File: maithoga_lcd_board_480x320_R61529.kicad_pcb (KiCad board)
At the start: 2 copper layers, 15 parts, among them P1 Display Connector, P2 40pin_fpc_top_0_5mm, U1 TSC2007, U2 DIO5661ST6

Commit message: Schematic ready, need check
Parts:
- added P3: TouchXY Connector, Goldpin:Goldpin_4_2_2_54mm_SMT, F.Cu at (138.4, 110.5)
- P2: value 40pin_fpc_top_0_5mm -> LicheePi_Con
- moved U1 24.8 mm to (177.8, 88.3)
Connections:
- C3 pad 1: /Display and Touchscreen/LCD Backlight/LCD_LED_A -> /Display and Touchscreen/LCD_LED_A
- D2 pad 1: /Display and Touchscreen/LCD Backlight/LCD_LED_A -> /Display and Touchscreen/LCD_LED_A
- DIS1 pad 1: /Display and Touchscreen/LCD Backlight/LCD_LED_K -> /Display and Touchscreen/LCD_LED_K
- DIS1 pad 11: (no net) -> /Display and Touchscreen/DISP_TE
- DIS1 pad 12: (no net) -> /Display and Touchscreen/DISP_~CS~
- DIS1 pad 13: (no net) -> /Display and Touchscreen/DISP_RS
- DIS1 pad 14: (no net) -> /Display and Touchscreen/DISP_~WR~
- DIS1 pad 15: (no net) -> /Display and Touchscreen/DISP_~RD~
- DIS1 pad 16: (no net) -> /Display and Touchscreen/DISP_SDA
- DIS1 pad 17: (no net) -> /Display and Touchscreen/DISP_SDO
- DIS1 pad 18: (no net) -> /Display and Touchscreen/DISP_D0
- DIS1 pad 19: (no net) -> /Display and Touchscreen/DISP_D1
- DIS1 pad 2: /Display and Touchscreen/LCD Backlight/LCD_LED_K -> /Display and Touchscreen/LCD_LED_K
- DIS1 pad 20: (no net) -> /Display and Touchscreen/DISP_D2
- DIS1 pad 21: (no net) -> /Display and Touchscreen/DISP_D3
- DIS1 pad 22: (no net) -> /Display and Touchscreen/DISP_D4
- DIS1 pad 23: (no net) -> /Display and Touchscreen/DISP_D5
- DIS1 pad 24: (no net) -> /Display and Touchscreen/DISP_D6
- DIS1 pad 25: (no net) -> /Display and Touchscreen/DISP_D7
- DIS1 pad 26: (no net) -> /Display and Touchscreen/DISP_D8
- DIS1 pad 27: (no net) -> /Display and Touchscreen/DISP_D9
- DIS1 pad 28: (no net) -> /Display and Touchscreen/DISP_D10
- DIS1 pad 29: (no net) -> /Display and Touchscreen/DISP_D11
- DIS1 pad 3: /Display and Touchscreen/LCD Backlight/LCD_LED_K -> /Display and Touchscreen/LCD_LED_K
- DIS1 pad 30: (no net) -> /Display and Touchscreen/DISP_D12
- DIS1 pad 31: (no net) -> /Display and Touchscreen/DISP_D13
- DIS1 pad 32: (no net) -> /Display and Touchscreen/DISP_D14
- DIS1 pad 33: (no net) -> /Display and Touchscreen/DISP_D15
- DIS1 pad 34: (no net) -> /Display and Touchscreen/DISP_D16
- DIS1 pad 35: (no net) -> /Display and Touchscreen/DISP_D17
- DIS1 pad 36: (no net) -> /Display and Touchscreen/DISP_ENABLE
- DIS1 pad 37: (no net) -> /Display and Touchscreen/DISP_DOTCLK
- DIS1 pad 38: (no net) -> /Display and Touchscreen/DISP_HSYNC
- DIS1 pad 4: /Display and Touchscreen/LCD Backlight/LCD_LED_K -> /Display and Touchscreen/LCD_LED_K
- DIS1 pad 40: (no net) -> /Display and Touchscreen/DISP_VSYNC
- DIS1 pad 41: (no net) -> /Display and Touchscreen/DISP_~RESET~
- DIS1 pad 46: Net-(DIS1-Pad46) -> /Lichee Pi Display Connector/TPX1
- DIS1 pad 47: Net-(DIS1-Pad47) -> /Lichee Pi Display Connector/TPX2
- DIS1 pad 48: Net-(DIS1-Pad48) -> /Lichee Pi Display Connector/TPY1
- DIS1 pad 49: Net-(DIS1-Pad49) -> /Lichee Pi Display Connector/TPY2
- DIS1 pad 5: /Display and Touchscreen/LCD Backlight/LCD_LED_K -> /Display and Touchscreen/LCD_LED_K
- DIS1 pad 6: /Display and Touchscreen/LCD Backlight/LCD_LED_K -> /Display and Touchscreen/LCD_LED_K
- DIS1 pad 7: /Display and Touchscreen/LCD Backlight/LCD_LED_A -> /Display and Touchscreen/LCD_LED_A
- P1 pad 1: (no net) -> 3V3
- P1 pad 10: (no net) -> /Display and Touchscreen/DISP_SDA
- P1 pad 11: (no net) -> /Display and Touchscreen/DISP_SDO
- P1 pad 12: (no net) -> /Display and Touchscreen/DISP_D0
- P1 pad 13: (no net) -> /Display and Touchscreen/DISP_D1
- P1 pad 14: (no net) -> /Display and Touchscreen/DISP_D2
- P1 pad 15: (no net) -> /Display and Touchscreen/DISP_D3
- P1 pad 16: (no net) -> /Display and Touchscreen/DISP_D4
- P1 pad 17: (no net) -> /Display and Touchscreen/DISP_D5
- P1 pad 18: (no net) -> /Display and Touchscreen/DISP_D6
- P1 pad 19: (no net) -> /Display and Touchscreen/DISP_D7
- P1 pad 2: (no net) -> GND
- P1 pad 20: (no net) -> /Display and Touchscreen/DISP_D8
- P1 pad 21: (no net) -> /Display and Touchscreen/DISP_D9
- P1 pad 22: (no net) -> /Display and Touchscreen/DISP_D10
- P1 pad 23: (no net) -> /Display and Touchscreen/DISP_D11
- P1 pad 24: (no net) -> /Display and Touchscreen/DISP_D12
- P1 pad 25: (no net) -> /Display and Touchscreen/DISP_D13
- P1 pad 26: (no net) -> /Display and Touchscreen/DISP_D14
- P1 pad 27: (no net) -> /Display and Touchscreen/DISP_D15
- P1 pad 28: (no net) -> /Display and Touchscreen/DISP_D16
- P1 pad 29: (no net) -> /Display and Touchscreen/DISP_D17
- P1 pad 3: (no net) -> /Display and Touchscreen/LCD_LED_K
- P1 pad 30: (no net) -> /Display and Touchscreen/DISP_ENABLE
- P1 pad 31: (no net) -> /Display and Touchscreen/DISP_DOTCLK
- P1 pad 32: (no net) -> /Display and Touchscreen/DISP_HSYNC
- P1 pad 33: (no net) -> /Display and Touchscreen/DISP_VSYNC
- P1 pad 34: (no net) -> /Display and Touchscreen/DISP_~RESET~
- P1 pad 35: (no net) -> /Display and Touchscreen/TOUCHSCREEN_SDA
- P1 pad 36: (no net) -> /Display and Touchscreen/TOUCHSCREEN_SCL
- P1 pad 37: (no net) -> 3V3
- P1 pad 38: (no net) -> GND
- P1 pad 39: (no net) -> /Display and Touchscreen/TOUCHSCREEN_IRQ
- P1 pad 4: (no net) -> /Display and Touchscreen/LCD_LED_A
- P1 pad 40: (no net) -> /Display and Touchscreen/BACKLIGHT_PWM
- P1 pad 5: (no net) -> /Display and Touchscreen/DISP_TE
- P1 pad 6: (no net) -> /Display and Touchscreen/DISP_~CS~
- P1 pad 7: (no net) -> /Display and Touchscreen/DISP_RS
- P1 pad 8: (no net) -> /Display and Touchscreen/DISP_~WR~
- P1 pad 9: (no net) -> /Display and Touchscreen/DISP_~RD~
- P2 pad 1: (no net) -> /Display and Touchscreen/LCD_LED_K
- P2 pad 10: (no net) -> /Display and Touchscreen/DISP_D3
- P2 pad 11: (no net) -> /Display and Touchscreen/DISP_D4
- P2 pad 12: (no net) -> /Display and Touchscreen/DISP_D5
- P2 pad 13: (no net) -> GND
- P2 pad 14: (no net) -> GND
- P2 pad 15: (no net) -> /Display and Touchscreen/DISP_D6
- P2 pad 16: (no net) -> /Display and Touchscreen/DISP_D7
- P2 pad 17: (no net) -> /Display and Touchscreen/DISP_D8
- P2 pad 18: (no net) -> /Display and Touchscreen/DISP_D9
- P2 pad 19: (no net) -> /Display and Touchscreen/DISP_D10
- P2 pad 2: (no net) -> /Display and Touchscreen/LCD_LED_A
- P2 pad 20: (no net) -> /Display and Touchscreen/DISP_D11
- P2 pad 21: (no net) -> GND
- P2 pad 22: (no net) -> GND
- P2 pad 23: (no net) -> /Display and Touchscreen/DISP_D12
- P2 pad 24: (no net) -> /Display and Touchscreen/DISP_D13
- P2 pad 25: (no net) -> /Display and Touchscreen/DISP_D14
- P2 pad 26: (no net) -> /Display and Touchscreen/DISP_D15
- P2 pad 27: (no net) -> /Display and Touchscreen/DISP_D16
- P2 pad 28: (no net) -> /Display and Touchscreen/DISP_D17
- P2 pad 29: (no net) -> GND
- P2 pad 3: (no net) -> GND
- P2 pad 30: (no net) -> /Display and Touchscreen/DISP_DOTCLK
- P2 pad 31: (no net) -> 3V3
- P2 pad 32: (no net) -> /Display and Touchscreen/DISP_HSYNC
- P2 pad 33: (no net) -> /Display and Touchscreen/DISP_VSYNC
- P2 pad 34: (no net) -> /Display and Touchscreen/DISP_ENABLE
- P2 pad 36: (no net) -> GND
- P2 pad 37: (no net) -> /Lichee Pi Display Connector/TPX1
- P2 pad 38: (no net) -> /Lichee Pi Display Connector/TPY1
- P2 pad 39: (no net) -> /Lichee Pi Display Connector/TPX2
- P2 pad 4: (no net) -> 3V3
- P2 pad 40: (no net) -> /Lichee Pi Display Connector/TPY2
- P2 pad 5: (no net) -> GND
- P2 pad 6: (no net) -> GND
- P2 pad 7: (no net) -> /Display and Touchscreen/DISP_D0
- P2 pad 8: (no net) -> /Display and Touchscreen/DISP_D1
- P2 pad 9: (no net) -> /Display and Touchscreen/DISP_D2
- R4 pad 1: /Display and Touchscreen/LCD Backlight/LCD_LED_K -> /Display and Touchscreen/LCD_LED_K
- U1 pad 2: Net-(DIS1-Pad46) -> /Lichee Pi Display Connector/TPX1
- U1 pad 3: Net-(DIS1-Pad48) -> /Lichee Pi Display Connector/TPY1
- U1 pad 4: Net-(DIS1-Pad47) -> /Lichee Pi Display Connector/TPX2
- U1 pad 5: Net-(DIS1-Pad49) -> /Lichee Pi Display Connector/TPY2
- U2 pad 3: /Display and Touchscreen/LCD Backlight/LCD_LED_K -> /Display and Touchscreen/LCD_LED_K
- U2 pad 4: (no net) -> /Display and Touchscreen/BACKLIGHT_PWM

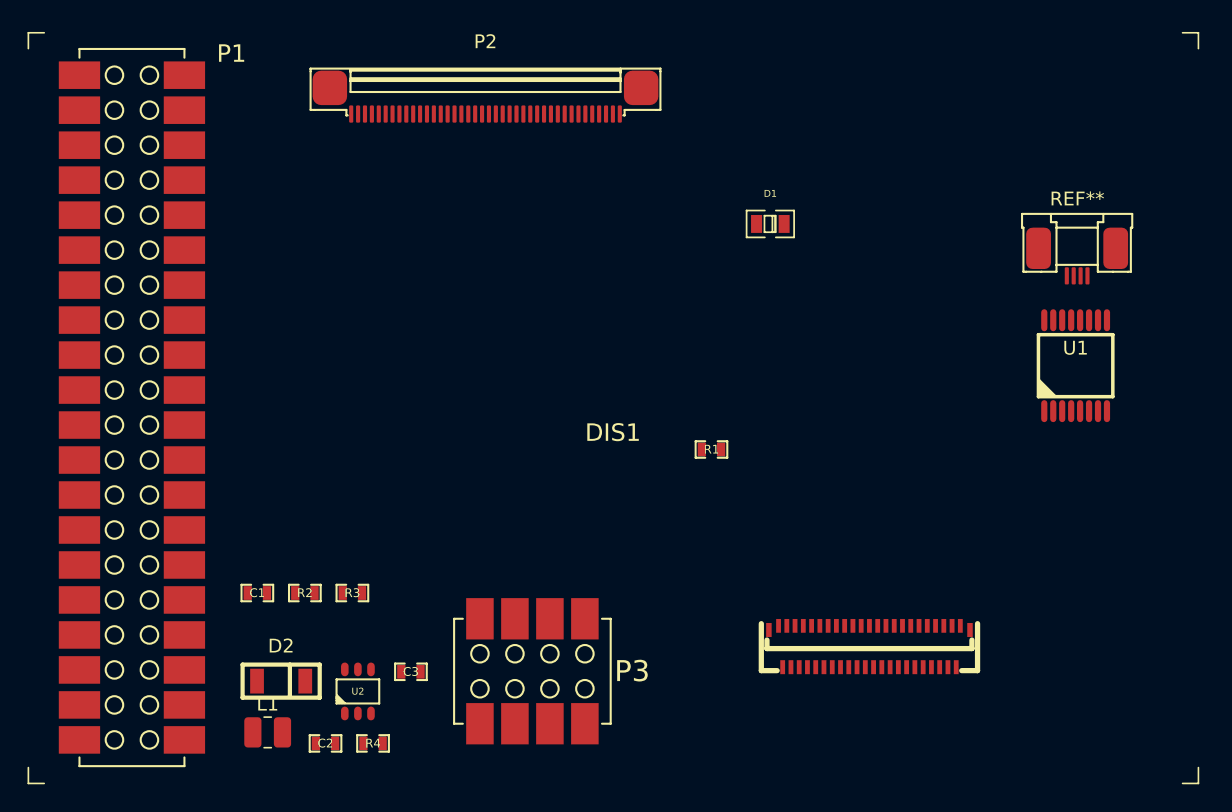
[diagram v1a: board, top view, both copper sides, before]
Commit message: Schematic finished, pcb tracking started
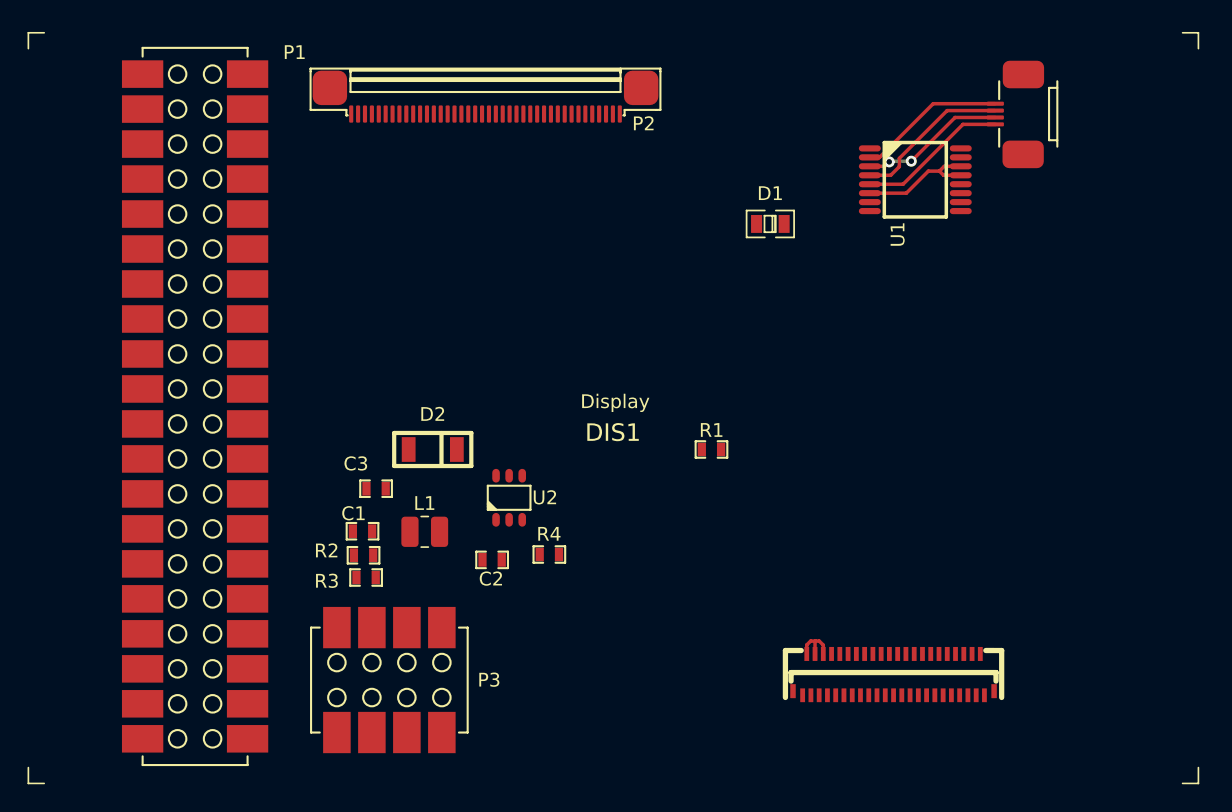
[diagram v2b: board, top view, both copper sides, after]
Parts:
- moved D2 20.1 mm to (131.2, 94.4)
- moved R4 18.8 mm to (139.6, 102.0)
- moved L1 18.5 mm to (130.6, 100.4)
- moved C2 18.0 mm to (135.5, 102.4)
- moved U2 17.8 mm to (136.7, 97.9)
- moved U1 17.8 mm to (166.2, 74.8), turned to 270 degrees
- moved C3 13.5 mm to (127.0, 97.3)
- moved P3 10.4 mm to (128.0, 111.2)
- moved C1 8.85 mm to (126.0, 100.3)
- moved R2 5.07 mm to (126.1, 102.1)
- moved P1 4.59 mm to (113.9, 91.3)
- moved R3 1.50 mm to (126.3, 103.7)
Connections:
- P2 pad 1: /Display and Touchscreen/LCD_LED_K -> /Lichee Pi Display Connector/TPY2
- P2 pad 10: /Display and Touchscreen/DISP_D3 -> 3V3
- P2 pad 11: /Display and Touchscreen/DISP_D4 -> /Display and Touchscreen/DISP_DOTCLK
- P2 pad 12: /Display and Touchscreen/DISP_D5 -> GND
- P2 pad 13: GND -> /Display and Touchscreen/DISP_D17
- P2 pad 14: GND -> /Display and Touchscreen/DISP_D16
- P2 pad 15: /Display and Touchscreen/DISP_D6 -> /Display and Touchscreen/DISP_D15
- P2 pad 16: /Display and Touchscreen/DISP_D7 -> /Display and Touchscreen/DISP_D14
- P2 pad 17: /Display and Touchscreen/DISP_D8 -> /Display and Touchscreen/DISP_D13
- P2 pad 18: /Display and Touchscreen/DISP_D9 -> /Display and Touchscreen/DISP_D12
- P2 pad 19: /Display and Touchscreen/DISP_D10 -> GND
- P2 pad 2: /Display and Touchscreen/LCD_LED_A -> /Lichee Pi Display Connector/TPX2
- P2 pad 20: /Display and Touchscreen/DISP_D11 -> GND
- P2 pad 21: GND -> /Display and Touchscreen/DISP_D11
- P2 pad 22: GND -> /Display and Touchscreen/DISP_D10
- P2 pad 23: /Display and Touchscreen/DISP_D12 -> /Display and Touchscreen/DISP_D9
- P2 pad 24: /Display and Touchscreen/DISP_D13 -> /Display and Touchscreen/DISP_D8
- P2 pad 25: /Display and Touchscreen/DISP_D14 -> /Display and Touchscreen/DISP_D7
- P2 pad 26: /Display and Touchscreen/DISP_D15 -> /Display and Touchscreen/DISP_D6
- P2 pad 27: /Display and Touchscreen/DISP_D16 -> GND
- P2 pad 28: /Display and Touchscreen/DISP_D17 -> GND
- P2 pad 29: GND -> /Display and Touchscreen/DISP_D5
- P2 pad 3: GND -> /Lichee Pi Display Connector/TPY1
- P2 pad 30: /Display and Touchscreen/DISP_DOTCLK -> /Display and Touchscreen/DISP_D4
- P2 pad 31: 3V3 -> /Display and Touchscreen/DISP_D3
- P2 pad 32: /Display and Touchscreen/DISP_HSYNC -> /Display and Touchscreen/DISP_D2
- P2 pad 33: /Display and Touchscreen/DISP_VSYNC -> /Display and Touchscreen/DISP_D1
- P2 pad 34: /Display and Touchscreen/DISP_ENABLE -> /Display and Touchscreen/DISP_D0
- P2 pad 35: (no net) -> GND
- P2 pad 37: /Lichee Pi Display Connector/TPX1 -> 3V3
- P2 pad 38: /Lichee Pi Display Connector/TPY1 -> GND
- P2 pad 39: /Lichee Pi Display Connector/TPX2 -> /Display and Touchscreen/LCD_LED_A
- P2 pad 4: 3V3 -> /Lichee Pi Display Connector/TPX1
- P2 pad 40: /Lichee Pi Display Connector/TPY2 -> /Display and Touchscreen/LCD_LED_K
- P2 pad 6: GND -> (no net)
- P2 pad 7: /Display and Touchscreen/DISP_D0 -> /Display and Touchscreen/DISP_ENABLE
- P2 pad 8: /Display and Touchscreen/DISP_D1 -> /Display and Touchscreen/DISP_VSYNC
- P2 pad 9: /Display and Touchscreen/DISP_D2 -> /Display and Touchscreen/DISP_HSYNC
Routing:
- net /Lichee Pi Display Connector/TPX2: track 0.00 -> 11.4 mm
- net /Lichee Pi Display Connector/TPY2: track 0.00 -> 10.9 mm
- net /Lichee Pi Display Connector/TPX1: track 0.00 -> 10.7 mm
- net /Lichee Pi Display Connector/TPY1: track 0.00 -> 10.6 mm, vias 0 -> 2
- net GND: track 0.00 -> 9.08 mm
- net /Display and Touchscreen/LCD_LED_K: track 0.00 -> 3.69 mm
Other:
- net class Default: trace_width 0.25 -> 0.254

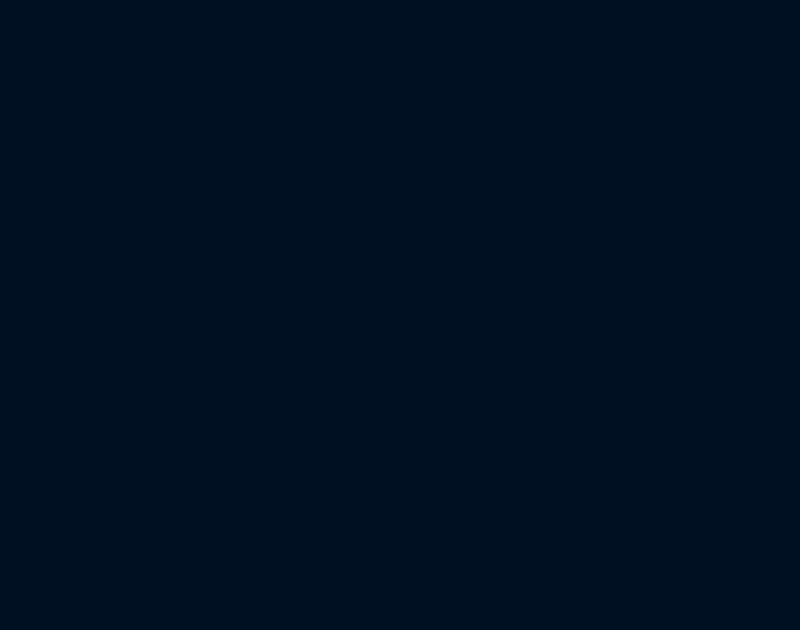
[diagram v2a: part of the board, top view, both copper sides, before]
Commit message: Added resistor mode select on schematic
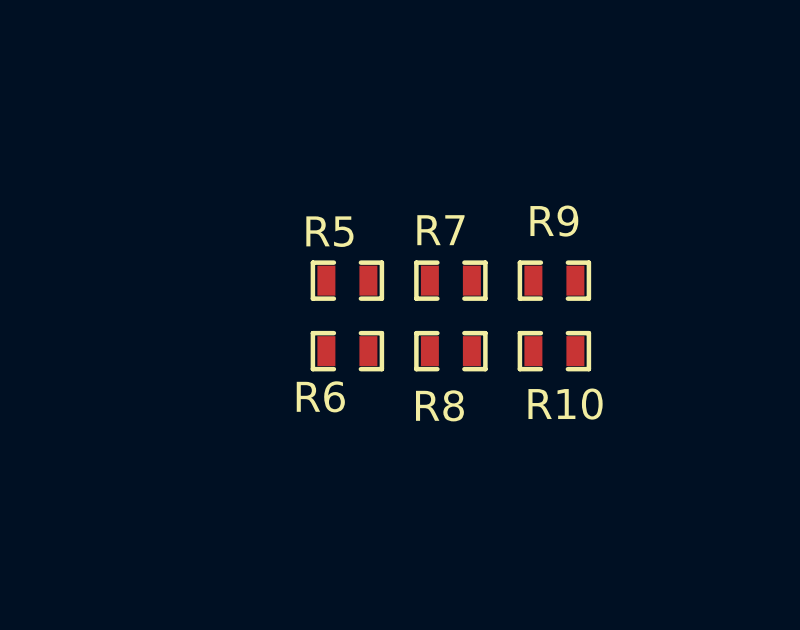
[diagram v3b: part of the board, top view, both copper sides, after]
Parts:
- added R10: 0R, Resistor_Smd_0603:0R_0603, F.Cu at (180.6, 98.0)
- added R5: 0R_NA, Resistor_Smd_0603:0R_0603, F.Cu at (173.7, 95.7)
- added R6: 0R_NA, Resistor_Smd_0603:0R_0603, F.Cu at (173.7, 98.0)
- added R7: 0R, Resistor_Smd_0603:0R_0603, F.Cu at (177.2, 95.7)
- added R8: 0R_NA, Resistor_Smd_0603:0R_0603, F.Cu at (177.2, 98.0)
- added R9: 0R, Resistor_Smd_0603:0R_0603, F.Cu at (180.6, 95.7)
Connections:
- DIS1 pad 42: Net-(D1-Pad2) -> Net-(DIS1-Pad42)
- DIS1 pad 43: Net-(D1-Pad2) -> Net-(DIS1-Pad43)
- DIS1 pad 44: GND -> Net-(DIS1-Pad44)

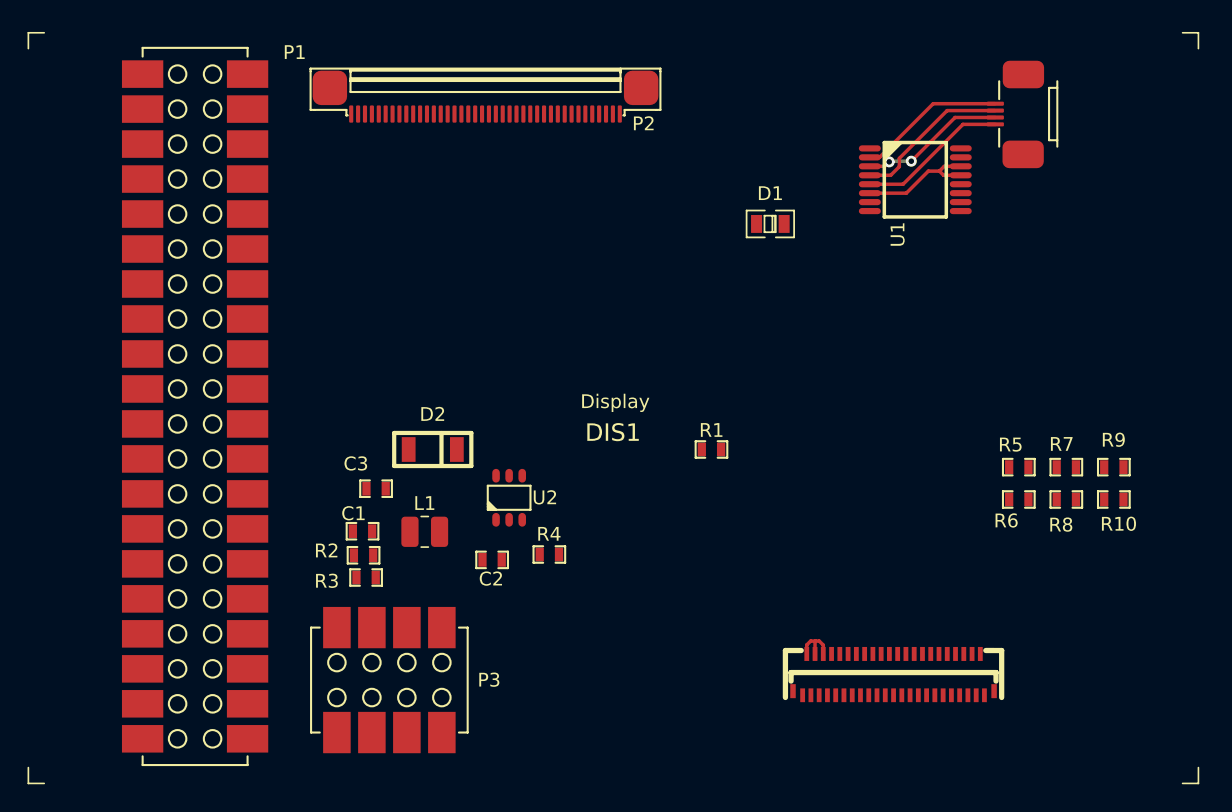
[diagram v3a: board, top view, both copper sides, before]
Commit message: Added outline on pcb
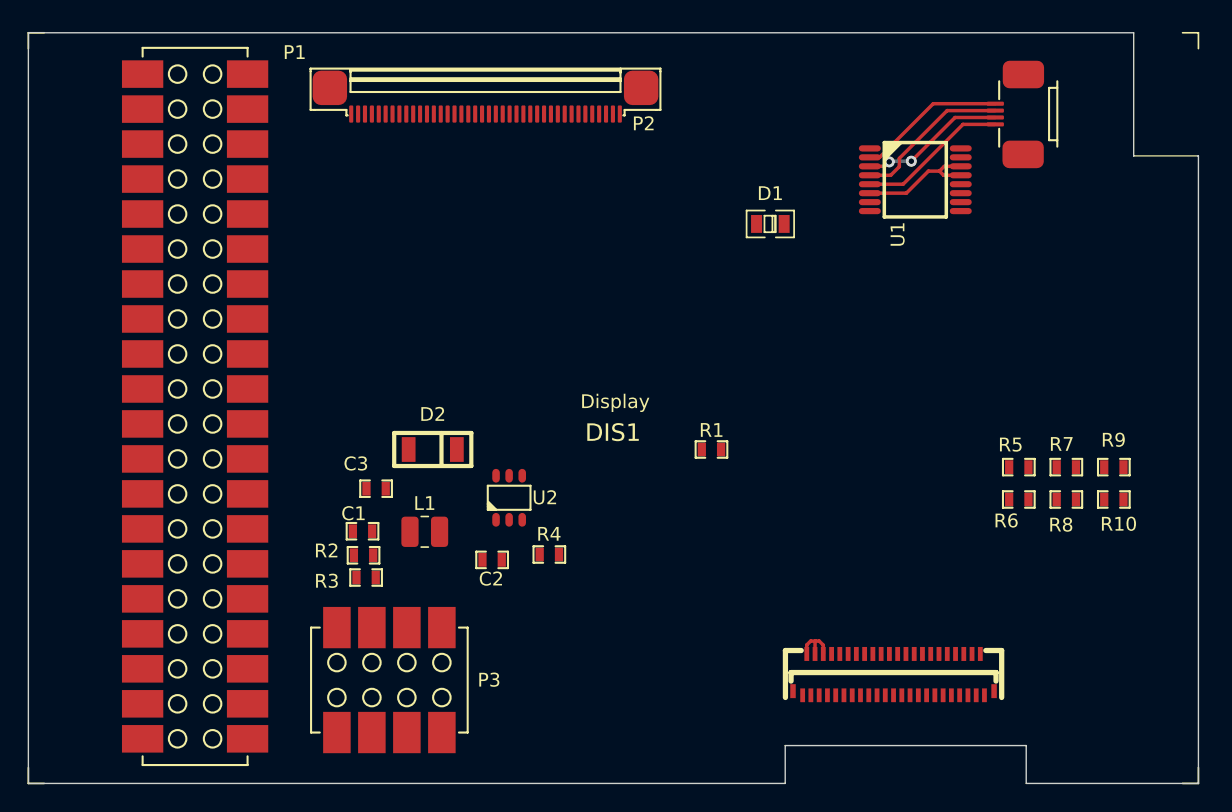
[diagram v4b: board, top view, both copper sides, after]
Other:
- board outline added: 85 x 54.5 mm

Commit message: Tracking in progress
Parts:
- moved R2 51.8 mm to (171.3, 76.7), turned to 90 degrees
- moved R3 49.3 mm to (168.6, 78.4)
- moved C1 46.4 mm to (161.9, 71.0), turned to 90 degrees
- moved C3 31.7 mm to (155.8, 110.4), turned to 90 degrees
- moved D1 28.2 mm to (162.1, 105.5), turned to 270 degrees
- moved R1 27.7 mm to (172.7, 76.7), turned to 90 degrees
- moved D2 27.1 mm to (153.8, 109.4), turned to 270 degrees
- moved L1 23.5 mm to (153.8, 104.3), turned to 270 degrees
- moved U2 22.2 mm to (157.6, 105.3)
- moved C2 21.5 mm to (156.9, 101.9), turned to 270 degrees
- moved R4 20.9 mm to (160.0, 106.6), turned to 270 degrees
- moved R9 12.2 mm to (171.8, 104.1), turned to 90 degrees
- moved R10 11.9 mm to (170.4, 104.1), turned to 90 degrees
- moved R8 7.25 mm to (173.1, 104.1), turned to 90 degrees
- moved R7 7.14 mm to (173.1, 101.6), turned to 90 degrees
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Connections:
- P3 pad 7: GND -> 3V3
- P3 pad 8: 3V3 -> GND
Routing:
- net /Display and Touchscreen/DISP_DOTCLK: track 0.00 -> 64.1 mm, vias 0 -> 2
- net /Display and Touchscreen/DISP_ENABLE: track 0.00 -> 63.5 mm, vias 0 -> 2
- net /Display and Touchscreen/DISP_HSYNC: track 0.00 -> 63.2 mm, vias 0 -> 2
- net /Display and Touchscreen/DISP_VSYNC: track 0.00 -> 63.0 mm, vias 0 -> 2
- net /Display and Touchscreen/DISP_D17: track 0.00 -> 62.7 mm, vias 0 -> 2
- net Net-(D1-Pad2): track 0.00 -> 18.4 mm
- net 3V3: track 0.00 -> 15.9 mm
- net GND: track 9.08 -> 21.0 mm
- net Net-(DIS1-Pad43): track 0.00 -> 11.0 mm, vias 0 -> 2
- net /Display and Touchscreen/LCD_LED_K: track 3.69 -> 14.6 mm
- net /Display and Touchscreen/LCD_LED_A: track 0.00 -> 8.60 mm
- net Net-(DIS1-Pad44): track 0.00 -> 8.55 mm, vias 0 -> 2
- net Net-(DIS1-Pad42): track 0.00 -> 7.82 mm, vias 0 -> 2
- net Net-(D2-Pad2): track 0.00 -> 6.12 mm
- net /Display and Touchscreen/TOUCHSCREEN_SCL: track 0.00 -> 3.80 mm
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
